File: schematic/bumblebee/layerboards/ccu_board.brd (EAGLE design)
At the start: 85 x 25 mm, 11 parts

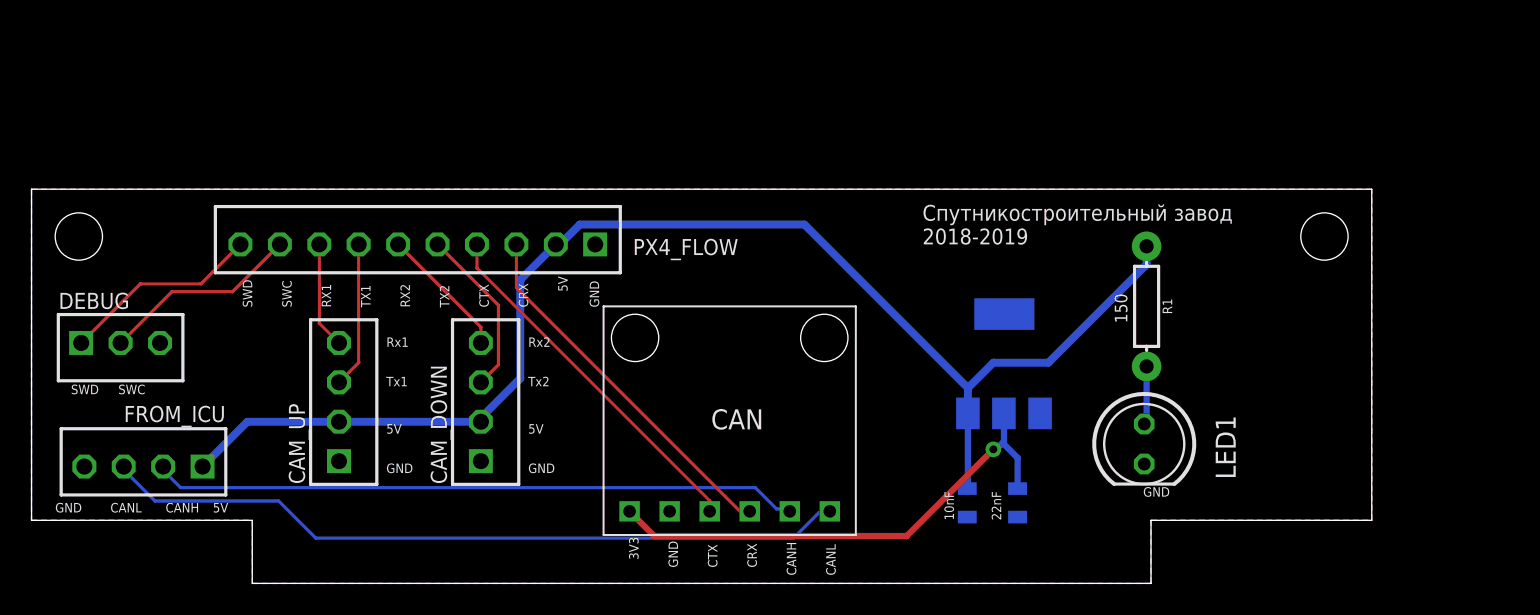
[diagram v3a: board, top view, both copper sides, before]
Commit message: Добавлена плата АЦП на CCU Сделана и разведена внешняя плата Кое-что сделал в либе
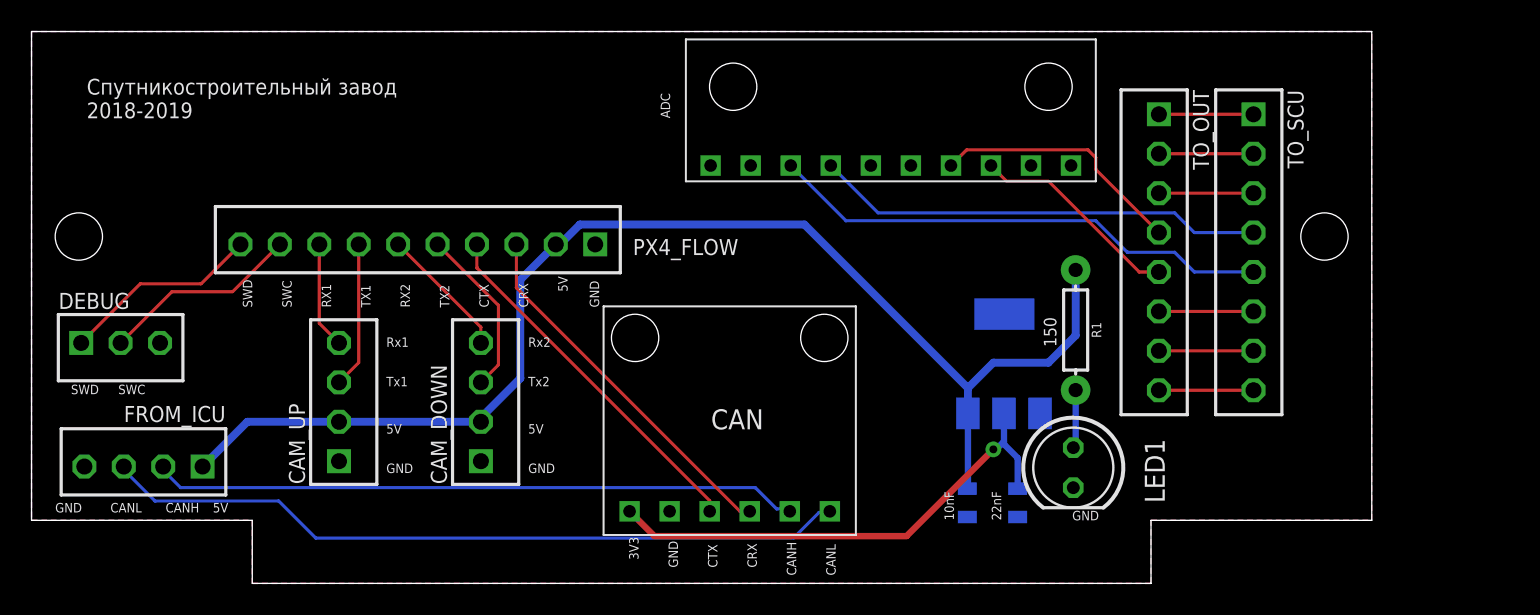
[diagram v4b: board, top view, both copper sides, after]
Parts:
- added TO_OUT, TO_SCU: B8B-EH-A, con-jst-eh:B8B-EH-A
- added U$1: ADS, bluepill:ADS
- moved LED1 4.74 mm to (66.1, 7.34)
- moved R1 4.74 mm to (66.2, 16.1)
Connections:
- new net N$1: TO_OUT.8, TO_SCU.8
- new net N$10: TO_SCU.4, U$1.SDA
- new net N$12: TO_OUT.5, U$1.A1
- new net N$13: TO_OUT.4, U$1.A0
- new net N$2: TO_OUT.7, TO_SCU.7
- new net N$3: TO_OUT.6, TO_SCU.6
- new net N$4: TO_OUT.3, TO_SCU.3
- new net N$5: TO_OUT.2, TO_SCU.2
- new net N$7: TO_OUT.1, TO_SCU.1
- new net N$9: TO_SCU.5, U$1.SCL
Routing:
- net N$9: track 0.00 -> 32.1 mm
- net N$10: track 0.00 -> 28.6 mm
- net N$13: track 0.00 -> 16.2 mm
- net N$12: track 0.00 -> 13.4 mm
- net N$7: track 0.00 -> 6.00 mm
- net N$5: track 0.00 -> 6.00 mm
- net N$4: track 0.00 -> 6.00 mm
- net N$3: track 0.00 -> 6.00 mm
- net N$2: track 0.00 -> 6.00 mm
- net N$1: track 0.00 -> 6.00 mm
- net 5V_CCU: track 85.1 -> 81.8 mm
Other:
- board size 85 x 25 mm -> 85 x 35 mm
- board text added: "ADC"
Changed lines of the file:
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@@
 <?xml version="1.0" encoding="utf-8"?>
 <!DOCTYPE eagle SYSTEM "eagle.dtd">
-<eagle version="9.3.2">
+<eagle version="9.3.0">
 <drawing>
 <settings>
@@
 <plain>
 <wire x1="14" y1="0" x2="71" y2="0" width="0" layer="20"/>
-<wire x1="85" y1="4" x2="85" y2="25" width="0" layer="20"/>
-<wire x1="85" y1="25" x2="0" y2="25" width="0" layer="20"/>
-<wire x1="0" y1="25" x2="0" y2="4" width="0" layer="20"/>
+<wire x1="85" y1="4" x2="85" y2="35" width="0" layer="20"/>
+<wire x1="85" y1="35" x2="0" y2="35" width="0" layer="20"/>
+<wire x1="0" y1="35" x2="0" y2="4" width="0" layer="20"/>
 <wire x1="0" y1="4" x2="14" y2="4" width="0" layer="20"/>
 <wire x1="14" y1="4" x2="14" y2="0" width="0" layer="20"/>
@@
 <text x="48.5" y="0.5" size="0.6" layer="21" rot="R90">CANH</text>
 <text x="51" y="0.5" size="0.6" layer="21" rot="R90">CANL</text>
-<text x="69.5" y="16.5" size="0.8" layer="21" rot="R90">150</text>
+<text x="65" y="15" size="0.8" layer="21" rot="R90">150</text>
 <text x="58.5" y="4" size="0.6" layer="21" rot="R90">10nF</text>
 <text x="61.5" y="4" size="0.6" layer="21" rot="R90">22nF</text>
@@
 <text x="8.5" y="4.5" size="0.6" layer="21">CANH</text>
 <text x="5" y="4.5" size="0.6" layer="21">CANL</text>
-<text x="70.5" y="5.5" size="0.6" layer="21">GND</text>
-<text x="56.5" y="21.5" size="1" layer="21">Спутникостроительный завод
+<text x="66" y="4" size="0.6" layer="21">GND</text>
+<text x="3.5" y="29.5" size="1" layer="21">Спутникостроительный завод
 2018-2019</text>
+<text x="40.5" y="29.5" size="0.6" layer="21" rot="R90">ADC</text>
 </plain>
 <attributes>
@@
 <attribute name="VALUE" x="60.239" y="5.11" size="0.6096" layer="28" font="vector" ratio="20" rot="MR270" align="top-center"/>
 </element>
-<element name="LED1" library="led" library_urn="urn:adsk.eagle:library:259" package="LED5MM" package3d_urn="urn:adsk.eagle:package:15799/2" value="" x="70.57" y="8.84" smashed="yes" rot="R270">
-<attribute name="NAME" x="75.1034" y="10.665" size="1.27" layer="25" ratio="10" rot="R270"/>
-<attribute name="VALUE" x="68.7666" y="5.6396" size="1.27" layer="27" ratio="10" rot="R270"/>
-</element>
-<element name="R1" library="SparkFun-Resistors" package="AXIAL-0.3" value="150" x="70.72" y="17.57" smashed="yes" rot="R270">
-<attribute name="NAME" x="71.736" y="17.57" size="0.6096" layer="25" font="vector" ratio="20" rot="R270" align="bottom-center"/>
-<attribute name="PROD_ID" value=" " x="70.72" y="17.57" size="1.778" layer="27" rot="R270" display="off"/>
-<attribute name="VALUE" x="69.704" y="17.57" size="0.6096" layer="27" font="vector" ratio="20" rot="R270" align="top-center"/>
+<element name="LED1" library="led" library_urn="urn:adsk.eagle:library:259" package="LED5MM" package3d_urn="urn:adsk.eagle:package:15799/2" value="" x="66.07" y="7.34" smashed="yes" rot="R270">
+<attribute name="NAME" x="70.6034" y="9.165" size="1.27" layer="25" ratio="10" rot="R270"/>
+<attribute name="VALUE" x="64.2666" y="4.1396" size="1.27" layer="27" ratio="10" rot="R270"/>
+</element>
+<element name="R1" library="SparkFun-Resistors" package="AXIAL-0.3" value="150" x="66.22" y="16.07" smashed="yes" rot="R270">
+<attribute name="NAME" x="67.236" y="16.07" size="0.6096" layer="25" font="vector" ratio="20" rot="R270" align="bottom-center"/>
+<attribute name="PROD_ID" value=" " x="66.22" y="16.07" size="1.778" layer="27" rot="R270" display="off"/>
+<attribute name="VALUE" x="65.204" y="16.07" size="0.6096" layer="27" font="vector" ratio="20" rot="R270" align="top-center"/>
 </element>
 <element name="DEBUG" library="con-jst-eh" package="B3B-EH-A" value="B3B-EH-A" x="5.65" y="15.25" smashed="yes">
@@
 <attribute name="NAME" x="26.341" y="6.293" size="1.016" layer="25" ratio="18" rot="R90"/>
 <attribute name="VALUE" x="32.183" y="6.293" size="1.016" layer="27" ratio="10" rot="R90"/>
+</element>
+<element name="TO_SCU" library="con-jst-eh" package="B8B-EH-A" value="B8B-EH-A" x="77.5" y="21" smashed="yes" rot="R270">
+<attribute name="NAME" x="79.659" y="31.287" size="1.016" layer="25" ratio="18" rot="R270"/>
+<attribute name="VALUE" x="73.817" y="31.287" size="1.016" layer="27" ratio="10" rot="R270"/>
+</element>
+<element name="TO_OUT" library="con-jst-eh" package="B8B-EH-A" value="B8B-EH-A" x="71.5" y="21" smashed="yes" rot="R270">
+<attribute name="NAME" x="73.659" y="31.287" size="1.016" layer="25" ratio="18" rot="R270"/>
+<attribute name="VALUE" x="67.817" y="31.287" size="1.016" layer="27" ratio="10" rot="R270"/>
+</element>
+<element name="U$1" library="bluepill" package="ADS" value="ADS" x="54.5" y="30" smashed="yes" rot="R90">
+<attribute name="VALUE" x="71.01" y="26.19" size="1.27" layer="27" rot="R90"/>
 </element>
 </elements>
@@
 <wire x1="59.3886" y1="12.3886" x2="61" y2="14" width="0.5" layer="16"/>
 <wire x1="61" y1="14" x2="64.5" y2="14" width="0.5" layer="16"/>
-<wire x1="64.5" y1="14" x2="70.72" y2="20.22" width="0.5" layer="16"/>
-<wire x1="70.72" y1="20.22" x2="70.72" y2="21.38" width="0.5" layer="16"/>
 <wire x1="33.25" y1="21.5" x2="31" y2="19.25" width="0.5" layer="16"/>
 <wire x1="31" y1="19.25" x2="31" y2="13" width="0.5" layer="16"/>
@@
 <wire x1="19.5" y1="10.25" x2="13.69" y2="10.25" width="0.5" layer="16"/>
 <wire x1="13.69" y1="10.25" x2="10.85" y2="7.41" width="0.5" layer="16"/>
+<wire x1="64.5" y1="14" x2="66.22" y2="15.72" width="0.5" layer="16"/>
+<wire x1="66.22" y1="15.72" x2="66.22" y2="19.88" width="0.5" layer="16"/>
 </signal>
 <signal name="GND">
@@
 <contactref element="LED1" pad="K"/>
 <contactref element="CAN" pad="GND"/>
-<polygon width="0.2" layer="16">
-<vertex x="0" y="25"/>
+<contactref element="PX4_FLOW" pad="1"/>
+<contactref element="CAM_UP" pad="1"/>
+<contactref element="CAM_DOWN" pad="1"/>
+<polygon width="0.1524" layer="1">
+<vertex x="0" y="35"/>
 <vertex x="0" y="4"/>
 <vertex x="14" y="4"/>
@@
 <vertex x="71" y="4"/>
 <vertex x="85" y="4"/>
-<vertex x="85" y="25"/>
+<vertex x="85" y="35"/>
 </polygon>
-<polygon width="0.2" layer="1">
-<vertex x="0" y="25"/>
+<polygon width="0.1524" layer="16">
+<vertex x="0" y="35"/>
 <vertex x="0" y="4"/>
 <vertex x="14" y="4"/>
@@
 <vertex x="71" y="4"/>
 <vertex x="85" y="4"/>
-<vertex x="85" y="25"/>
+<vertex x="85" y="35"/>
 </polygon>
-<contactref element="PX4_FLOW" pad="1"/>
-<contactref element="CAM_UP" pad="1"/>
-<contactref element="CAM_DOWN" pad="1"/>
 </signal>
 <signal name="N$6">
@@
 <contactref element="LED1" pad="A"/>
 <contactref element="R1" pad="P$2"/>
-<wire x1="70.72" y1="13.76" x2="70.72" y2="10.26" width="0.4" layer="16"/>
-<wire x1="70.72" y1="10.26" x2="70.57" y2="10.11" width="0.4" layer="16"/>
+<wire x1="66.22" y1="12.26" x2="66.22" y2="8.76" width="0.4" layer="16"/>
+<wire x1="66.22" y1="8.76" x2="66.07" y2="8.61" width="0.4" layer="16"/>
 </signal>
 <signal name="RX1">
@@
 <wire x1="28.5" y1="16.25" x2="28.5" y2="15.25" width="0.2" layer="1"/>
 </signal>
+<signal name="N$1">
+<contactref element="TO_SCU" pad="8"/>
+<contactref element="TO_OUT" pad="8"/>
+<wire x1="71.5" y1="12.25" x2="77.5" y2="12.25" width="0.2" layer="1"/>
+</signal>
+<signal name="N$2">
+<contactref element="TO_SCU" pad="7"/>
+<contactref element="TO_OUT" pad="7"/>
+<wire x1="71.5" y1="14.75" x2="77.5" y2="14.75" width="0.2" layer="1"/>
+</signal>
+<signal name="N$3">
+<contactref element="TO_SCU" pad="6"/>
+<contactref element="TO_OUT" pad="6"/>
+<wire x1="71.5" y1="17.25" x2="77.5" y2="17.25" width="0.2" layer="1"/>
+</signal>
+<signal name="N$4">
+<contactref element="TO_SCU" pad="3"/>
+<contactref element="TO_OUT" pad="3"/>
+<wire x1="71.5" y1="24.75" x2="77.5" y2="24.75" width="0.2" layer="1"/>
+</signal>
+<signal name="N$5">
+<contactref element="TO_SCU" pad="2"/>
+<contactref element="TO_OUT" pad="2"/>
+<wire x1="71.5" y1="27.25" x2="77.5" y2="27.25" width="0.2" layer="1"/>
+</signal>
+<signal name="N$7">
+<contactref element="TO_SCU" pad="1"/>
+<contactref element="TO_OUT" pad="1"/>
+<wire x1="71.5" y1="29.75" x2="77.5" y2="29.75" width="0.2" layer="1"/>
+</signal>
+<signal name="N$9">
+<contactref element="TO_SCU" pad="5"/>
+<contactref element="U$1" pad="SCL"/>
+<wire x1="77.5" y1="19.75" x2="73.75" y2="19.75" width="0.2" layer="16"/>
+<wire x1="72.5" y1="21" x2="69.5" y2="21" width="0.2" layer="16"/>
+<wire x1="69.5" y1="21" x2="67.5" y2="23" width="0.2" layer="16"/>
+<wire x1="67.5" y1="23" x2="51.65" y2="23" width="0.2" layer="16"/>
+<wire x1="51.65" y1="23" x2="48.15" y2="26.5" width="0.2" layer="16"/>
+<wire x1="73.75" y1="19.75" x2="72.5" y2="21" width="0.2" layer="16"/>
+</signal>
+<signal name="N$10">
+<contactref element="TO_SCU" pad="4"/>
+<contactref element="U$1" pad="SDA"/>
+<wire x1="77.5" y1="22.25" x2="73.75" y2="22.25" width="0.2" layer="16"/>
+<wire x1="53.69" y1="23.5" x2="50.69" y2="26.5" width="0.2" layer="16"/>
+<wire x1="73.75" y1="22.25" x2="72.5" y2="23.5" width="0.2" layer="16"/>
+<wire x1="72.5" y1="23.5" x2="53.69" y2="23.5" width="0.2" layer="16"/>
+</signal>
+<signal name="N$12">
+<contactref element="TO_OUT" pad="5"/>
+<contactref element="U$1" pad="A1"/>
+<wire x1="71.5" y1="19.75" x2="70.25" y2="19.75" width="0.2" layer="1"/>
+<wire x1="61.85" y1="25.5" x2="60.85" y2="26.5" width="0.2" layer="1"/>
+<wire x1="70.25" y1="19.75" x2="64.5" y2="25.5" width="0.2" layer="1"/>
+<wire x1="64.5" y1="25.5" x2="61.85" y2="25.5" width="0.2" layer="1"/>
+</signal>
+<signal name="N$13">
+<contactref element="TO_OUT" pad="4"/>
+<contactref element="U$1" pad="A0"/>
+<wire x1="71.5" y1="22.25" x2="67.5" y2="26.25" width="0.2" layer="1"/>
+<wire x1="67.5" y1="26.25" x2="67.5" y2="27" width="0.2" layer="1"/>
+<wire x1="67.5" y1="27" x2="67" y2="27.5" width="0.2" layer="1"/>
+<wire x1="59.31" y1="27.5" x2="58.31" y2="26.5" width="0.2" layer="1"/>
+<wire x1="67" y1="27.5" x2="59.31" y2="27.5" width="0.2" layer="1"/>
+</signal>
 </signals>
